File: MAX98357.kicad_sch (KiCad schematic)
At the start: 20 parts, among them J11 AudioJack3, J8 SPKR, U10 PCM5102A, U6 MAX98357AETE_

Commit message: relayout SDRAM
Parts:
- C50, C51, C52, C53, C54, C56, C58: footprint (none) -> Capacitor_SMD:C_0603_1608Metric
- C55, C57, C59: footprint (none) -> Capacitor_SMD:C_0402_1005Metric
- J11: footprint (none) -> Connector_Audio:Jack_3.5mm_CUI_SJ-3523-SMT_Horizontal
- R37, R38: footprint (none) -> Resistor_SMD:R_0603_1608Metric
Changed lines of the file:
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@@
 		(shape input)
 		(at 95.25 59.69 180)
+		(fields_autoplaced yes)
 		(effects
 			(font
@@
 		(shape input)
 		(at 95.25 57.15 180)
+		(fields_autoplaced yes)
 		(effects
 			(font
@@
 		(shape input)
 		(at 95.25 54.61 180)
+		(fields_autoplaced yes)
 		(effects
 			(font
@@
 			)
 		)
-		(property "Footprint" ""
+		(property "Footprint" "Capacitor_SMD:C_0603_1608Metric"
 			(at 140.6652 86.36 0)
 			(effects
@@
 			)
 		)
-		(property "Footprint" ""
+		(property "Footprint" "Capacitor_SMD:C_0402_1005Metric"
 			(at 171.45 33.02 0)
 			(effects
@@
 			)
 		)
-		(property "Footprint" ""
+		(property "Footprint" "Capacitor_SMD:C_0603_1608Metric"
 			(at 168.6052 69.85 0)
 			(effects
@@
 			)
 		)
-		(property "Footprint" ""
+		(property "Footprint" "Capacitor_SMD:C_0603_1608Metric"
 			(at 136.8552 36.83 0)
 			(effects
@@
 			)
 		)
-		(property "Footprint" ""
+		(property "Footprint" "Connector_Audio:Jack_3.5mm_CUI_SJ-3523-SMT_Horizontal"
 			(at 187.96 57.15 0)
 			(effects
@@
 			)
 		)
-		(property "Footprint" ""
+		(property "Footprint" "Capacitor_SMD:C_0603_1608Metric"
 			(at 100.0252 36.83 0)
 			(effects
@@
 			)
 		)
-		(property "Footprint" ""
+		(property "Footprint" "Resistor_SMD:R_0603_1608Metric"
 			(at 151.13 56.388 90)
 			(effects
@@
 			)
 		)
-		(property "Footprint" ""
+		(property "Footprint" "Capacitor_SMD:C_0603_1608Metric"
 			(at 157.1752 69.85 0)
 			(effects
@@
 			)
 		)
-		(property "Footprint" ""
+		(property "Footprint" "Capacitor_SMD:C_0603_1608Metric"
 			(at 140.6652 69.85 0)
 			(effects
@@
 			)
 		)
-		(property "Footprint" ""
+		(property "Footprint" "Resistor_SMD:R_0603_1608Metric"
 			(at 151.13 55.372 90)
 			(effects
@@
 			)
 		)
-		(property "Footprint" ""
+		(property "Footprint" "Capacitor_SMD:C_0402_1005Metric"
 			(at 147.32 33.02 0)
 			(effects
@@
 			)
 		)
-		(property "Footprint" ""
+		(property "Footprint" "Capacitor_SMD:C_0603_1608Metric"
 			(at 160.9852 36.83 0)
 			(effects
@@
 			)
 		)
-		(property "Footprint" ""
+		(property "Footprint" "Capacitor_SMD:C_0402_1005Metric"
 			(at 110.49 33.02 0)
 			(effects

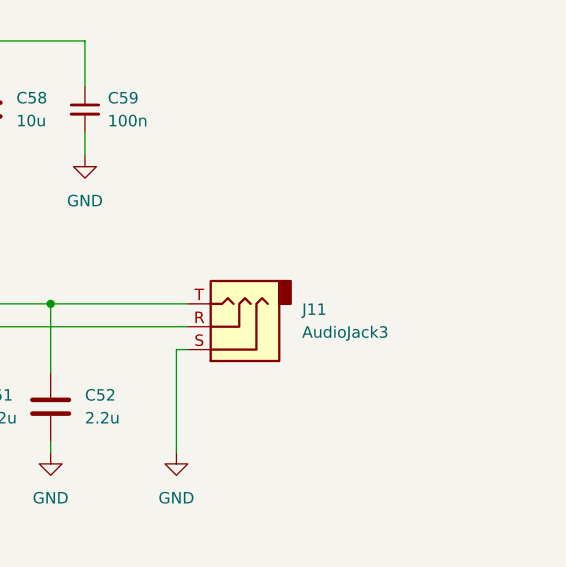
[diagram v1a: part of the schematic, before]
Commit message: Finished SDRAM, QSPI Flash, Planning to move to 5 inch orient display dimension
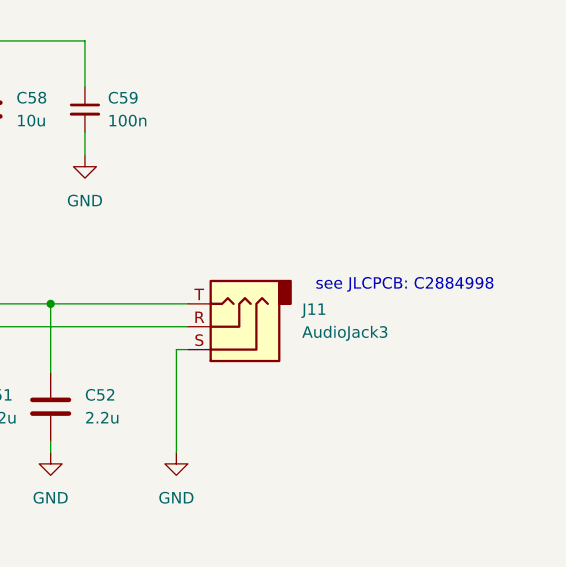
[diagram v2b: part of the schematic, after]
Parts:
- C50, C51, C52, C53: footprint Capacitor_SMD:C_0603_1608Metric -> Capacitor_SMD:C_0805_2012Metric; JLCPCB Part # (none) -> C377773
- C54, C56, C58: JLCPCB Part # (none) -> C96446
- C55, C57, C59: JLCPCB Part # (none) -> C307331
- J11: JLCPCB Part # (none) -> C2884998
- R37, R38: JLCPCB Part # (none) -> C23179
- U10: JLCPCB Part # (none) -> C107671
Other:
- note added: "see JLCPCB: C2884998"
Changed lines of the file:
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@@
 		)
 	)
+	(text "see JLCPCB: C2884998"
+		(exclude_from_sim no)
+		(at 207.01 52.578 0)
+		(effects
+			(font
+				(size 1.27 1.27)
+			)
+		)
+	)
 	(label "SPK+"
 		(at 166.37 135.89 180)
@@
 			)
 		)
-		(property "Footprint" "Capacitor_SMD:C_0603_1608Metric"
+		(property "Footprint" "Capacitor_SMD:C_0805_2012Metric"
 			(at 140.6652 86.36 0)
 			(effects
@@
 			)
 		)
+		(property "JLCPCB Part #" "C377773"
+			(at 139.7 82.55 0)
+			(effects
+				(font
+					(size 1.27 1.27)
+				)
+				(hide yes)
+			)
+		)
 		(pin "1"
 		)
@@
 			)
 		)
+		(property "JLCPCB Part #" "C307331"
+			(at 171.45 33.02 0)
+			(effects
+				(font
+					(size 1.27 1.27)
+				)
+				(hide yes)
+			)
+		)
 		(pin "1"
 		)
@@
 			)
 		)
-		(property "Footprint" "Capacitor_SMD:C_0603_1608Metric"
+		(property "Footprint" "Capacitor_SMD:C_0805_2012Metric"
 			(at 168.6052 69.85 0)
 			(effects
@@
 			)
 		)
+		(property "JLCPCB Part #" "C377773"
+			(at 167.64 66.04 0)
+			(effects
+				(font
+					(size 1.27 1.27)
+				)
+				(hide yes)
+			)
+		)
 		(pin "1"
 		)
@@
 			)
 		)
+		(property "JLCPCB Part #" "C96446"
+			(at 135.89 33.02 0)
+			(effects
+				(font
+					(size 1.27 1.27)
+				)
+				(hide yes)
+			)
+		)
 		(pin "1"
 		)
@@
 			)
 		)
+		(property "JLCPCB Part #" "C2884998"
+			(at 187.96 57.15 0)
+			(effects
+				(font
+					(size 1.27 1.27)
+				)
+				(hide yes)
+			)
+		)
 		(pin "R"
 		)
@@
 			)
 		)
+		(property "JLCPCB Part #" "C107671"
+			(at 121.92 64.77 0)
+			(effects
+				(font
+					(size 1.27 1.27)
+				)
+				(hide yes)
+			)
+		)
 		(pin "17"
 		)
@@
 			)
 		)
+		(property "JLCPCB Part #" "C96446"
+			(at 99.06 33.02 0)
+			(effects
+				(font
+					(size 1.27 1.27)
+				)
+				(hide yes)
+			)
+		)
 		(pin "1"
 		)
@@
 			)
 		)
+		(property "JLCPCB Part #" "C23179"
+			(at 151.13 54.61 0)
+			(effects
+				(font
+					(size 1.27 1.27)
+				)
+				(hide yes)
+			)
+		)
 		(pin "1"
 		)
@@
 			)
 		)
-		(property "Footprint" "Capacitor_SMD:C_0603_1608Metric"
+		(property "Footprint" "Capacitor_SMD:C_0805_2012Metric"
 			(at 157.1752 69.85 0)
 			(effects
@@
 			)
 		)
+		(property "JLCPCB Part #" "C377773"
+			(at 156.21 66.04 0)
+			(effects
+				(font
+					(size 1.27 1.27)
+				)
+				(hide yes)
+			)
+		)
 		(pin "1"
 		)
@@
 			)
 		)
-		(property "Footprint" "Capacitor_SMD:C_0603_1608Metric"
+		(property "Footprint" "Capacitor_SMD:C_0805_2012Metric"
 			(at 140.6652 69.85 0)
 			(effects
@@
 			)
 		)
+		(property "JLCPCB Part #" "C377773"
+			(at 139.7 66.04 0)
+			(effects
+				(font
+					(size 1.27 1.27)
+				)
+				(hide yes)
+			)
+		)
 		(pin "1"
 		)
@@
 			)
 		)
+		(property "JLCPCB Part #" "C23179"
+			(at 151.13 57.15 0)
+			(effects
+				(font
+					(size 1.27 1.27)
+				)
+				(hide yes)
+			)
+		)
 		(pin "1"
 		)
@@
 			)
 		)
+		(property "JLCPCB Part #" "C307331"
+			(at 147.32 33.02 0)
+			(effects
+				(font
+					(size 1.27 1.27)
+				)
+				(hide yes)
+			)
+		)
 		(pin "1"
 		)
@@
 			)
 		)
+		(property "JLCPCB Part #" "C96446"
+			(at 160.02 33.02 0)
+			(effects
+				(font
+					(size 1.27 1.27)
+				)
+				(hide yes)
+			)
+		)
 		(pin "1"
 		)
@@
 			(at 110.49 33.02 0)
 			(effects
+				(font
+					(size 1.27 1.27)
+				)
+				(hide yes)
+			)
+		)
+		(property "JLCPCB Part #" "C307331"
+			(at 110.49 33.02 0)
+			(effects
